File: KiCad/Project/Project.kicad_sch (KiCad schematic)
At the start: 19 parts, among them J5 USB_B, M1 Terminal_01x02, M2 Terminal_01x02, M3 Terminal_01x02, U1 ATmega328P-P, U2 HC-06, Y1 16Mhz

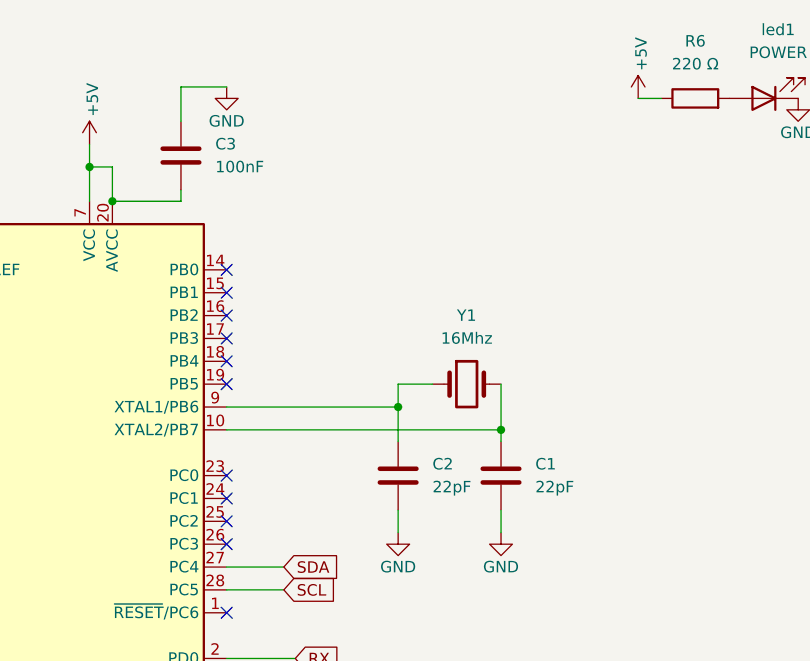
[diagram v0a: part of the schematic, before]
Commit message: v 1.4
updated capacitor values, for real this time
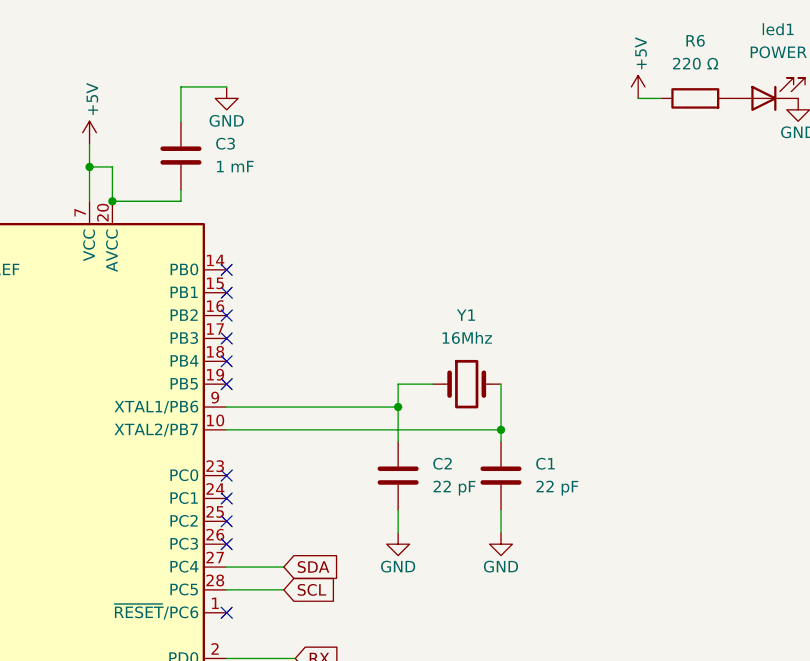
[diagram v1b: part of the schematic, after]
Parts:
- C1, C2: value 22pF -> 22 pF
- C3: value 100nF -> 1 mF
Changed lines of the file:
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@@
 		(fields_autoplaced yes)
 		(property "Reference" "C3"
-			(at 92.71 34.29 0)
+			(at 92.71 34.2899 0)
 			(effects
 				(font
@@
 			)
 		)
-		(property "Value" "100nF"
-			(at 92.71 36.83 0)
+		(property "Value" "1 mF"
+			(at 92.71 36.8299 0)
 			(effects
 				(font
@@
 		(fields_autoplaced yes)
 		(property "Reference" "C2"
-			(at 116.84 69.85 0)
+			(at 116.84 69.8499 0)
 			(effects
 				(font
@@
 			)
 		)
-		(property "Value" "22pF"
-			(at 116.84 72.39 0)
+		(property "Value" "22 pF"
+			(at 116.84 72.3899 0)
 			(effects
 				(font
@@
 		(fields_autoplaced yes)
 		(property "Reference" "C1"
-			(at 128.27 69.85 0)
+			(at 128.27 69.8499 0)
 			(effects
 				(font
@@
 			)
 		)
-		(property "Value" "22pF"
-			(at 128.27 72.39 0)
-			(effects
-				(font
+		(property "Value" "22 pF"
+			(at 128.27 72.3899 0)
+			(effects
+				(font
